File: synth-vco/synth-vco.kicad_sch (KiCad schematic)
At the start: 146 parts, among them J1 Conn_Coaxial, J2 Screw_Terminal_01x10, J3 Screw_Terminal_01x05, J4 Conn_Coaxial, J5 Barrel_Jack, U1 ADF4158, U10 LT3045IMSE_TRPBF, U11 LT3045IMSE_TRPBF, U12 LT3045IMSE_TRPBF, U13 LT8570EMS8E_TRPBF, U14 LT3065EDDPBF, U15 LT3065EDDPBF, U16 BT09E, U3 ADP-2-10+, U4 DAT-15R5A-SP+, U5 OPA192IDGKT, U6 TPSM53602RDAR, U7 LT3045IMSE_TRPBF, U8 LT3045IMSE_TRPBF, U9 LT3045IMSE_TRPBF, Y1 FT3MN 26 MHz, Y3 CVCO55CW-0500-1000

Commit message: refactor: switched from screw terminals to pin header
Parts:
- removed J2: Screw_Terminal_01x10, TerminalBlock_Phoenix:TerminalBlock_Phoenix_PT-1,5-10-3.5-H_1x10_P3.50mm_Horizontal, symbol Connector:Screw_Terminal_01x10
- removed J3: Screw_Terminal_01x05, TerminalBlock_Phoenix:TerminalBlock_Phoenix_PT-1,5-5-3.5-H_1x05_P3.50mm_Horizontal, symbol Connector:Screw_Terminal_01x05
- added J2: Conn_02x09_Odd_Even, Connector_PinHeader_2.54mm:PinHeader_2x09_P2.54mm_Vertical, symbol Connector_Generic:Conn_02x09_Odd_Even
- R28: renamed from R27; Tolerance (none) -> 0.1%
- R40: renamed from R28; Tolerance (none) -> 0.1%
- renumbered C45 to C1, C2 to C10, C3 to C11, C57 to C12, C59 to C13, C26 to C14, C58 to C15, C60 to C16, C28 to C17, C61 to C18, C63 to C19, C27 to C2, C62 to C20, C64 to C21, C4 to C22, C5 to C23, C29 to C24, C52 to C25, C6 to C26, C8 to C27, C23 to C28, C7 to C29, C46 to C3, C50 to C30, C51 to C31, C24 to C32, C30 to C33, C31 to C34, C9 to C35, C10 to C36, C11 to C37, C53 to C38, C32 to C39, C47 to C4, C12 to C40, C54 to C41, C33 to C42, C55 to C43, C34 to C44, C13 to C45, C35 to C46, C15 to C47, C14 to C48, C16 to C49, C25 to C5, C17 to C50, C36 to C51, C22 to C52, C37 to C53, C20 to C54, C38 to C55, C39 to C57, C21 to C58, C40 to C59, C48 to C6, C66 to C60, C67 to C61, C41 to C62, C68 to C63, C42 to C64, C69 to C65, C71 to C66, C72 to C67, C70 to C68, C43 to C69, C49 to C7, C44 to C70, C1 to C8, C65 to C9, J5 to J1, J1 to J3, L2 to L1, L3 to L2, L1 to L3, L5 to L4, L6 to L5, R30 to R1, R34 to R10, R35 to R11, R3 to R12, R4 to R13, R24 to R14, R5 to R15, R6 to R16, R7 to R17, R25 to R18, R36 to R19, R31 to R2, R37 to R20, R8 to R21, R9 to R22, R10 to R23, R12 to R24, R11 to R25, R13 to R26, R26 to R27, R20 to R29, R33 to R3, R21 to R30, R14 to R31, R18 to R32, R17 to R33, R16 to R34, R15 to R35, R19 to R36, R39 to R37, R40 to R38, R41 to R39, R32 to R4, R29 to R41, R38 to R5, R1 to R6, R22 to R7, R23 to R8, R2 to R9, U13 to U1, U3 to U10, U10 to U11, U4 to U12, U11 to U13, U16 to U14, U12 to U15, U6 to U2, U1 to U3, U14 to U4, U7 to U5, U5 to U6, U8 to U7, U15 to U8, Y3 to Y2
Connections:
- net ATT_CLK: now also J2.13 (Pin_13)
- net ATT_DATA: now also J2.15 (Pin_15)
- net ATT_LE: now also J2.17 (Pin_17)
- net GND: now also J2.10 (Pin_10), J2.12 (Pin_12), J2.14 (Pin_14), J2.16 (Pin_16), J2.18 (Pin_18), J2.2 (Pin_2), J2.4 (Pin_4), J2.6 (Pin_6), J2.8 (Pin_8)
- net PLL_CE: now also J2.7 (Pin_7)
- net PLL_LE: now also J2.5 (Pin_5)
- net PLL_MUXOUT: now also J2.11 (Pin_11)
- net PLL_TXDATA: now also J2.9 (Pin_9)
- net SPI_CLK: now also J2.1 (Pin_1)
- net SPI_DATA: now also J2.3 (Pin_3)

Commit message: fix: adl5611 footprint
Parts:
- renumbered C8 to C1, C36 to C10, C37 to C11, C40 to C12, C45 to C13, C48 to C14, C47 to C15, C49 to C16, C50 to C17, C10 to C2, C54 to C20, C58 to C21, C52 to C22, C28 to C23, C32 to C24, C5 to C25, C14 to C26, C2 to C27, C17 to C28, C24 to C29, C11 to C3, C33 to C30, C34 to C31, C39 to C32, C42 to C33, C44 to C34, C46 to C35, C51 to C36, C53 to C37, C55 to C38, C57 to C39, C22 to C4, C59 to C40, C62 to C41, C64 to C42, C69 to C43, C70 to C44, C1 to C45, C3 to C46, C4 to C47, C6 to C48, C7 to C49, C23 to C5, C30 to C50, C31 to C51, C25 to C52, C38 to C53, C41 to C54, C43 to C55, C12 to C57, C15 to C58, C13 to C59, C26 to C6, C16 to C60, C18 to C61, C20 to C62, C19 to C63, C21 to C64, C9 to C65, C60 to C66, C61 to C67, C63 to C68, C65 to C69, C29 to C7, C68 to C70, C66 to C71, C67 to C72, C27 to C8, C35 to C9, J3 to J1, J1 to J5, J2 to J6, L3 to L1, L1 to L2, L2 to L3, L4 to L5, L5 to L6, R6 to R1, R23 to R10, R25 to R11, R24 to R12, R26 to R13, R31 to R14, R35 to R15, R34 to R16, R33 to R17, R32 to R18, R36 to R19, R9 to R2, R29 to R20, R30 to R21, R7 to R22, R8 to R23, R14 to R24, R18 to R25, R27 to R26, R28 to R27, R40 to R28, R41 to R29, R12 to R3, R1 to R30, R2 to R31, R4 to R32, R3 to R33, R10 to R34, R11 to R35, R19 to R36, R20 to R37, R5 to R38, R37 to R39, R13 to R4, R38 to R40, R39 to R41, R15 to R5, R16 to R6, R17 to R7, R21 to R8, R22 to R9, U3 to U1, U11 to U10, U13 to U11, U15 to U12, U1 to U13, U4 to U14, U8 to U15, U14 to U16, U10 to U3, U12 to U4, U6 to U5, U2 to U6, U5 to U7, U7 to U8, Y2 to Y3

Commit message: refactor: changed barrel jack power input to screw terminal
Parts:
- removed J5: Barrel_Jack, Connector_BarrelJack:BarrelJack_SwitchcraftConxall_RAPC10U_Horizontal, symbol Connector:Barrel_Jack
- added J2: Screw_Terminal_01x02, TerminalBlock_CUI:TerminalBlock_CUI_TB007-508-02_1x02_P5.08mm_Horizontal, symbol Connector:Screw_Terminal_01x02
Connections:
- net +12V_IN: now also J2.2 (Pin_2)
- net GND: now also J2.1 (Pin_1)

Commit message: feat(power input): overvoltage and reverse polarity protection
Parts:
- added D3: WE-TVSP_DO, GPR_Radar_Footprints:WE-TVSP_DO-214AC_UNIDIRECTIONAL, symbol WE-TVSP_DO-214AC_400W_UNI:WE-TVSP_DO-214AC_400W_UNI
- added F1: MF-MSMF200, GPR_Radar_Footprints:FUSER_MF-MSMF200, symbol MF-MSMF200:MF-MSMF200
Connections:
- net +12V_IN: now also D3.1, F1.2; no longer J2.2 (Pin_2)
- net GND: now also D3.2
- new net: F1.1, J2.2 (Pin_2)
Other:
- moved on the sheet: C23, C24, C25, C26, C27, C28, C29, C30, C31, C32, C33, C34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

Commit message: feat: initial pcb layout
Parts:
- removed R20: 10K, Resistor_SMD:R_0603_1608Metric_Pad0.98x0.95mm_HandSolder, symbol Device:R
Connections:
- net ATT_DATA: now also U4.3 (DATA)
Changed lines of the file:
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@@
 	(wire
 		(pts
-			(xy 549.91 293.37) (xy 552.45 293.37)
-		)
-		(stroke
-			(width 0)
-			(type default)
-		)
-	)
-	(wire
-		(pts
 			(xy 356.87 292.1) (xy 356.87 298.45)
 		)
@@
 	(wire
 		(pts
-			(xy 560.07 293.37) (xy 568.96 293.37)
-		)
-		(stroke
-			(width 0)
-			(type default)
-		)
-	)
-	(wire
-		(pts
 			(xy 775.97 55.88) (xy 775.97 53.34)
 		)
@@
 	)
 	(label "ATT_DATA"
-		(at 549.91 293.37 180)
+		(at 568.96 293.37 180)
 		(effects
 			(font
@@
 					(unit 1)
 				)
-			)
-		)
-	)
-	(symbol
-		(lib_id "Device:R")
-		(at 556.26 293.37 90)
-		(unit 1)
-		(body_style 1)
-		(exclude_from_sim no)
-		(in_bom yes)
-		(on_board yes)
-		(in_pos_files yes)
-		(dnp no)
-		(property "Reference" "R20"
-			(at 556.26 296.926 90)
-			(show_name no)
-			(do_not_autoplace no)
-			(effects
-				(font
-					(size 0.762 0.762)
-				)
-			)
-		)
-		(property "Value" "10K"
-			(at 556.26 295.656 90)
-			(show_name no)
-			(do_not_autoplace no)
-			(effects
-				(font
-					(size 0.762 0.762)
-				)
-			)
-		)
-		(property "Footprint" "Resistor_SMD:R_0603_1608Metric_Pad0.98x0.95mm_HandSolder"
-			(at 556.26 295.148 90)
-			(hide yes)
-			(show_name no)
-			(do_not_autoplace no)
-			(effects
-				(font
-					(size 1.27 1.27)
-				)
-			)
-		)
-		(property "Datasheet" ""
-			(at 556.26 293.37 0)
-			(hide yes)
-			(show_name no)
-			(do_not_autoplace no)
-			(effects
-				(font
-					(size 1.27 1.27)
-				)
-			)
-		)
-		(property "Description" "Resistor"
-			(at 556.26 293.37 0)
-			(hide yes)
-			(show_name no)
-			(do_not_autoplace no)
-			(effects
-				(font
-					(size 1.27 1.27)
-				)
-			)
-		)
-		(pin "1"
-		)
-		(pin "2"
-		)
-		(instances
-			(project "synth-vco"
-				(path "/73cd0915-f93d-4399-bfe5-6d917fa8cde7"
-					(reference "R20")
-					(unit 1)
-				)

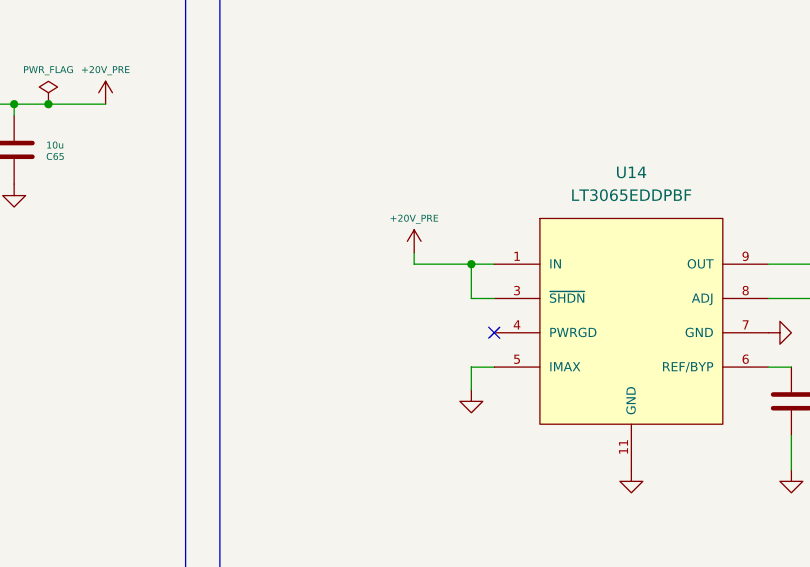
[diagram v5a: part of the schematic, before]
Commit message: feat(power blocks): pcb layout of power blocks
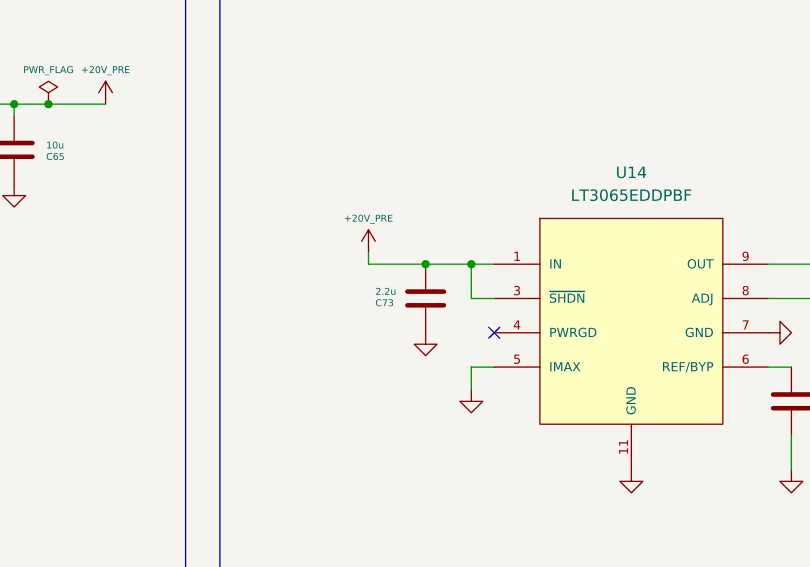
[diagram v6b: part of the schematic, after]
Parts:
- added C73: 2.2u, Capacitor_SMD:C_0805_2012Metric_Pad1.18x1.45mm_HandSolder, symbol Device:C
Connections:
- net +20V_PRE: now also C73.2
- net GND: now also C73.1
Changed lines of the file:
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@@
 	)
 	(junction
+		(at 170.18 156.21)
+		(diameter 0)
+		(color 0 0 0 0)
+	)
+	(junction
 		(at 331.47 55.88)
 		(diameter 0)
@@
 	(wire
 		(pts
+			(xy 170.18 156.21) (xy 175.26 156.21)
+		)
+		(stroke
+			(width 0)
+			(type default)
+		)
+	)
+	(wire
+		(pts
 			(xy 358.14 292.1) (xy 356.87 292.1)
 		)
@@
 	(wire
 		(pts
-			(xy 168.91 154.94) (xy 168.91 156.21)
+			(xy 163.83 154.94) (xy 163.83 156.21)
 		)
 		(stroke
@@
 	(wire
 		(pts
-			(xy 168.91 156.21) (xy 175.26 156.21)
+			(xy 163.83 156.21) (xy 170.18 156.21)
 		)
 		(stroke
@@
 	(symbol
 		(lib_id "power:GND")
+		(at 170.18 163.83 0)
+		(unit 1)
+		(body_style 1)
+		(exclude_from_sim no)
+		(in_bom yes)
+		(on_board yes)
+		(in_pos_files yes)
+		(dnp no)
+		(fields_autoplaced yes)
+		(property "Reference" "#PWR0164"
+			(at 170.18 170.18 0)
+			(hide yes)
+			(show_name no)
+			(do_not_autoplace no)
+			(effects
+				(font
+					(size 1.27 1.27)
+				)
+			)
+		)
+		(property "Value" "GND"
+			(at 170.18 168.91 0)
+			(hide yes)
+			(show_name no)
+			(do_not_autoplace no)
+			(effects
+				(font
+					(size 1.27 1.27)
+				)
+			)
+		)
+		(property "Footprint" ""
+			(at 170.18 163.83 0)
+			(hide yes)
+			(show_name no)
+			(do_not_autoplace no)
+			(effects
+				(font
+					(size 1.27 1.27)
+				)
+			)
+		)
+		(property "Datasheet" ""
+			(at 170.18 163.83 0)
+			(hide yes)
+			(show_name no)
+			(do_not_autoplace no)
+			(effects
+				(font
+					(size 1.27 1.27)
+				)
+			)
+		)
+		(property "Description" "Power symbol creates a global label with name \"GND\" , ground"
+			(at 170.18 163.83 0)
+			(hide yes)
+			(show_name no)
+			(do_not_autoplace no)
+			(effects
+				(font
+					(size 1.27 1.27)
+				)
+			)
+		)
+		(pin "1"
+		)
+		(instances
+			(project "synth-vco"
+				(path "/73cd0915-f93d-4399-bfe5-6d917fa8cde7"
+					(reference "#PWR0164")
+					(unit 1)
+				)
+			)
+		)
+	)
+	(symbol
+		(lib_id "power:GND")
 		(at 717.55 304.8 0)
 		(unit 1)
@@
 	(symbol
 		(lib_id "Device:C")
+		(at 170.18 160.02 180)
+		(unit 1)
+		(body_style 1)
+		(exclude_from_sim no)
+		(in_bom yes)
+		(on_board yes)
+		(in_pos_files yes)
+		(dnp no)
+		(property "Reference" "C73"
+			(at 164.592 160.528 0)
+			(show_name no)
+			(do_not_autoplace no)
+			(effects
+				(font
+					(size 0.762 0.762)
+				)
+				(justify right)
+			)
+		)
+		(property "Value" "2.2u"
+			(at 164.592 159.258 0)
+			(show_name no)
+			(do_not_autoplace no)
+			(effects
+				(font
+					(size 0.762 0.762)
+				)
+				(justify right)
+			)
+		)
+		(property "Footprint" "Capacitor_SMD:C_0805_2012Metric_Pad1.18x1.45mm_HandSolder"
+			(at 169.2148 156.21 0)
+			(hide yes)
+			(show_name no)
+			(do_not_autoplace no)
+			(effects
+				(font
+					(size 1.27 1.27)
+				)
+			)
+		)
+		(property "Datasheet" ""
+			(at 170.18 160.02 0)
+			(hide yes)
+			(show_name no)
+			(do_not_autoplace no)
+			(effects
+				(font
+					(size 1.27 1.27)
+				)
+			)
+		)
+		(property "Description" "Unpolarized capacitor"
+			(at 170.18 160.02 0)
+			(hide yes)
+			(show_name no)
+			(do_not_autoplace no)
+			(effects
+				(font
+					(size 1.27 1.27)
+				)
+			)
+		)
+		(pin "2"
+		)
+		(pin "1"
+		)
+		(instances
+			(project "synth-vco"
+				(path "/73cd0915-f93d-4399-bfe5-6d917fa8cde7"
+					(reference "C73")
+					(unit 1)
+				)
+			)
+		)
+	)
+	(symbol
+		(lib_id "Device:C")
 		(at 210.82 171.45 180)
 		(unit 1)
@@
 	(symbol
 		(lib_id "power:+5V")
-		(at 168.91 154.94 0)
+		(at 163.83 154.94 0)
 		(unit 1)
 		(body_style 1)
@@
 		(fields_autoplaced yes)
 		(property "Reference" "#PWR0128"
-			(at 168.91 158.75 0)
+			(at 163.83 158.75 0)
 			(hide yes)
 			(show_name no)
@@
 		)
 		(property "Value" "+20V_PRE"
-			(at 168.91 151.13 0)
+			(at 163.83 151.13 0)
 			(show_name no)
 			(do_not_autoplace no)
@@
 		)
 		(property "Footprint" ""
-			(at 168.91 154.94 0)
+			(at 163.83 154.94 0)
 			(hide yes)
 			(show_name no)
@@
 		)
 		(property "Datasheet" ""
-			(at 168.91 154.94 0)
+			(at 163.83 154.94 0)
 			(hide yes)
 			(show_name no)
@@
 		)
 		(property "Description" "Power symbol creates a global label with name \"+5V\""
-			(at 168.91 154.94 0)
+			(at 163.83 154.94 0)
 			(hide yes)
 			(show_name no)

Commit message: feat(rf layout): rf track pcb layout kind of completed
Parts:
- removed C21: 100pF, Capacitor_SMD:C_0603_1608Metric_Pad1.08x0.95mm_HandSolder, symbol Device:C
- removed R39, R41: 100, Resistor_SMD:R_0603_1608Metric_Pad0.98x0.95mm_HandSolder, symbol Device:R
- removed R40: 68, Resistor_SMD:R_0603_1608Metric_Pad0.98x0.95mm_HandSolder, symbol Device:R
- added C18: 100nF, Capacitor_SMD:C_0603_1608Metric_Pad1.08x0.95mm_HandSolder, symbol Device:C
- added C74: 2.2u, Capacitor_SMD:C_0805_2012Metric_Pad1.18x1.45mm_HandSolder, symbol Device:C
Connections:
- net +18V_OPA: now also C18.1
- net +20V_PRE: now also C74.2
- net GND: now also C18.2, C74.1
- net at C9.1, Y3.2 (VT): now also L3.1; no longer L3.2
- net at U4.14 (RFout): now also C66.1
- net at R7.2: now also L3.2; no longer L3.1
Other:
- moved on the sheet: C66, C67, C68, C69, C70, C71, C72, FL4, J4, L3, L5, L6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

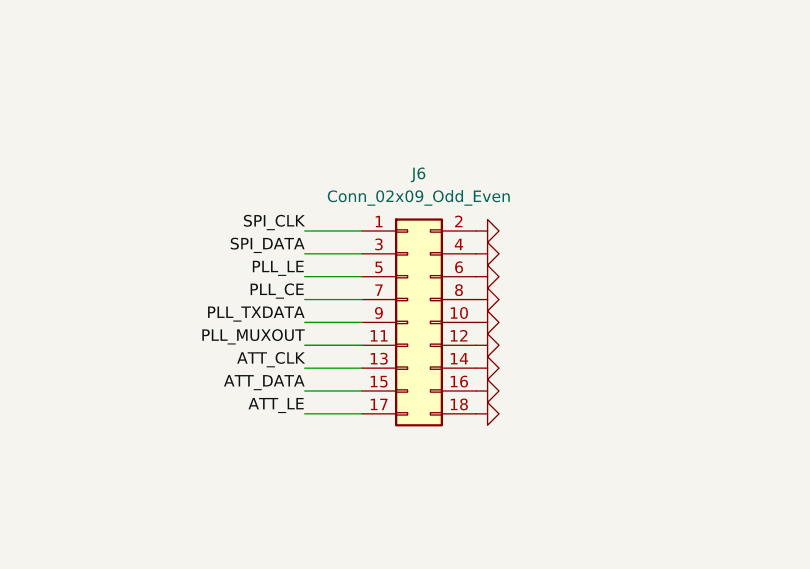
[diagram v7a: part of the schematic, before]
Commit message: refactor: switched to wurth box header
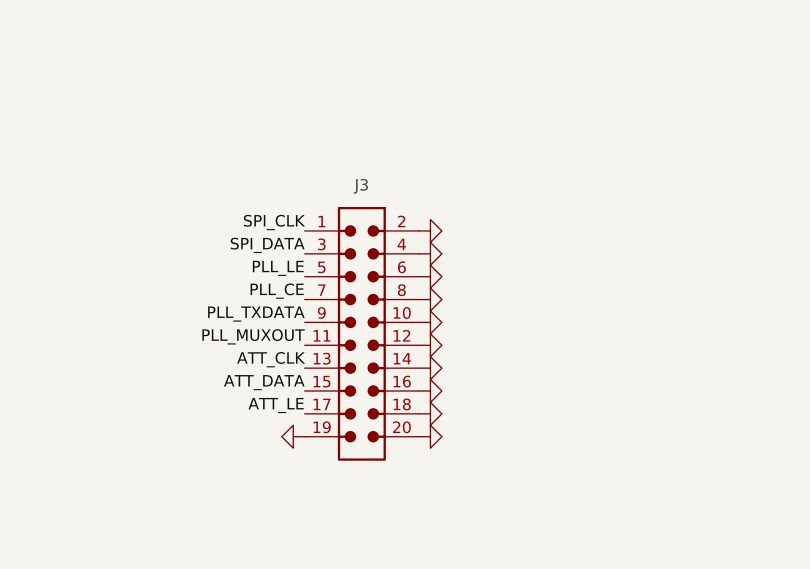
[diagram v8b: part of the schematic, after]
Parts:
- removed J6: Conn_02x09_Odd_Even, Connector_PinHeader_2.54mm:PinHeader_2x09_P2.54mm_Vertical, symbol Connector_Generic:Conn_02x09_Odd_Even
- added J3: 61202021621, GPR_Radar_Footprints:J_Wurth_WR-BHD_61202021621, symbol Connector_Wurth_WR-BHD:61202021621
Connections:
- net ATT_CLK: now also J3.13
- net ATT_DATA: now also J3.15
- net ATT_LE: now also J3.17
- net GND: now also J3.10, J3.12, J3.14, J3.16, J3.18, J3.19, J3.2, J3.20, J3.4, J3.6, J3.8
- net PLL_CE: now also J3.7
- net PLL_LE: now also J3.5
- net PLL_MUXOUT: now also J3.11
- net PLL_TXDATA: now also J3.9
- net SPI_CLK: now also J3.1
- net SPI_DATA: now also J3.3
